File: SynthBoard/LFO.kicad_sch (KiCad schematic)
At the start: 33 parts, among them IC1 PIC16F15325-I/P, IC2 MCP6232T-E/SN, IC3 MCP6232T-E/SN, J3 Input, J4 Output, Q1 Q_NPN_ECB, U1 NJM4558M

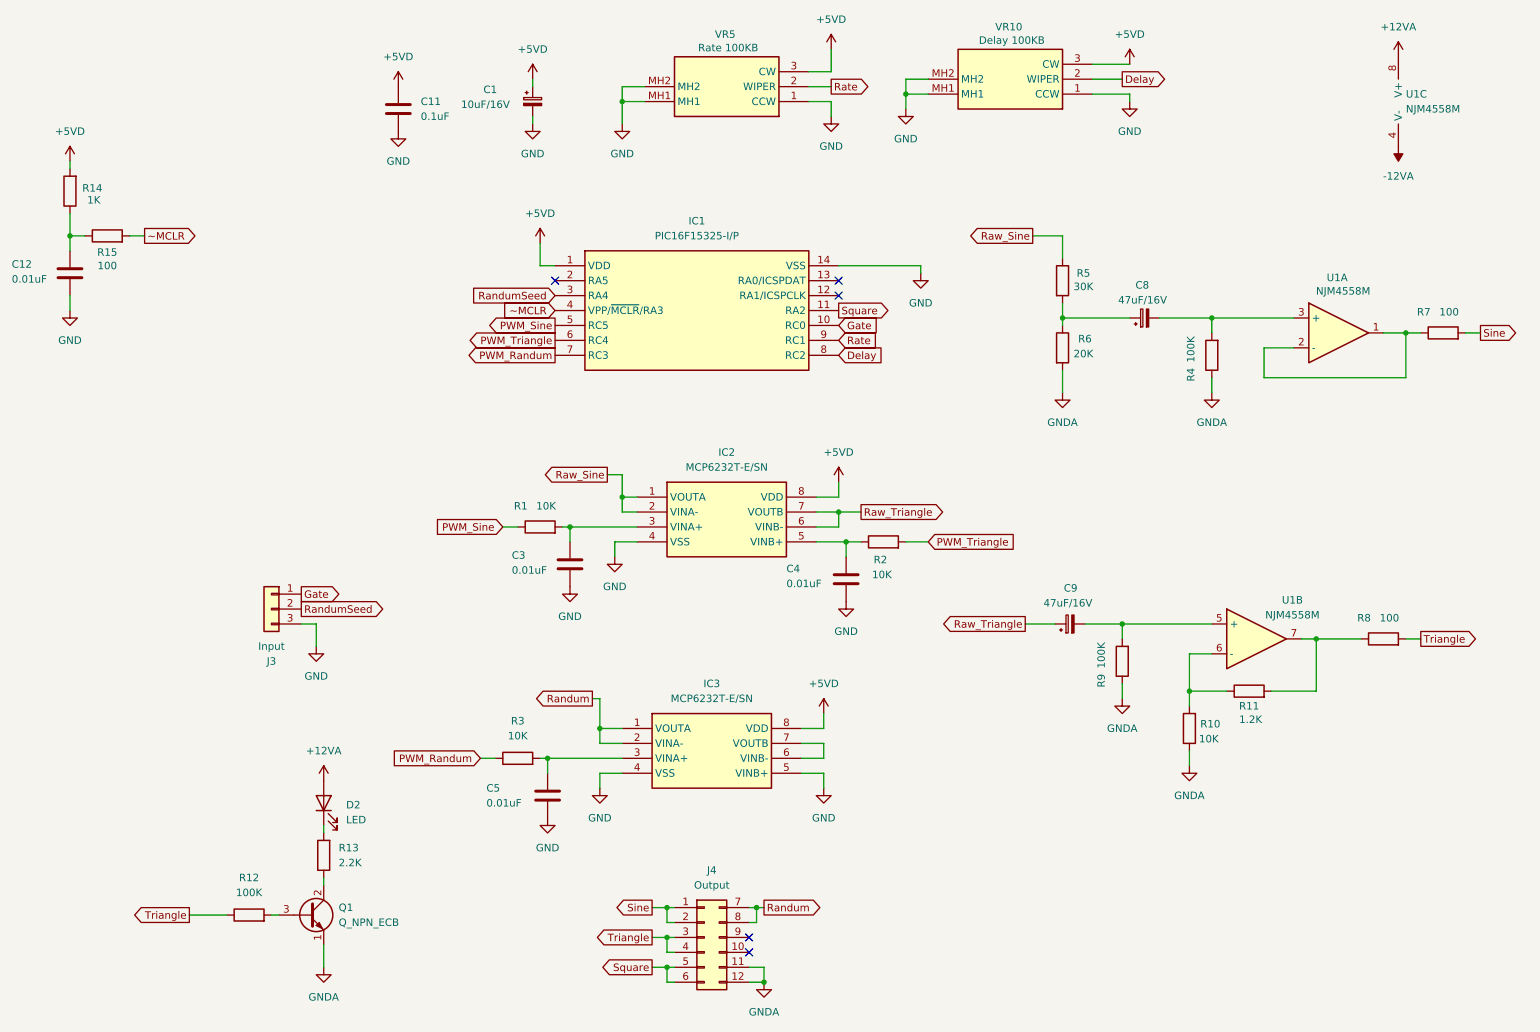
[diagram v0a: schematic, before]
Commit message: SynthBoard
部品をSMDにしてVCO+LFOを配置した
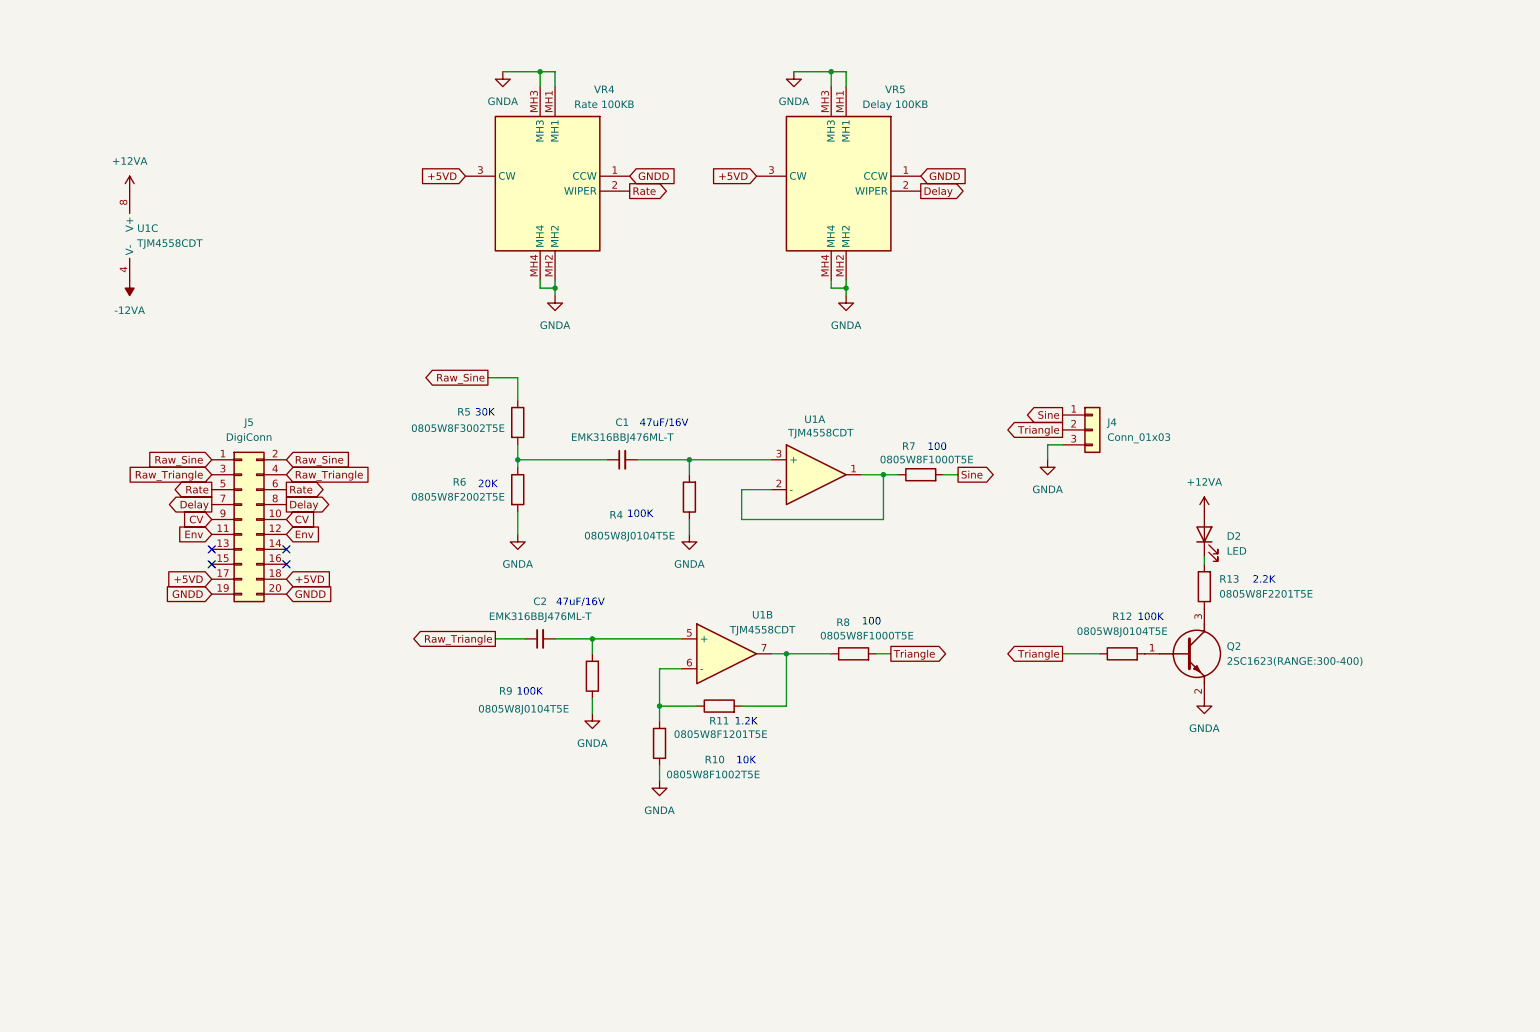
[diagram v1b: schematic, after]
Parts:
- removed C1: 10uF/16V, Capacitor_THT:CP_Radial_D5.0mm_P2.50mm, symbol Device:C_Polarized_Small
- removed C11: 0.1uF, Capacitor_SMD:C_0805_2012Metric_Pad1.18x1.45mm_HandSolder, symbol Device:C
- removed C12, C3, C4, C5: 0.01uF, Capacitor_THT:C_Disc_D7.5mm_W2.5mm_P5.00mm, symbol Device:C
- removed C8, C9: 47uF/16V, Capacitor_THT:CP_Radial_D5.0mm_P2.50mm, symbol Device:C_Polarized_Small
- removed IC1: PIC16F15325-I/P, Package_DIP:DIP-14_W7.62mm_LongPads, symbol SamacSys_Parts:PIC16F15325-I_P
- removed IC2, IC3: MCP6232T-E/SN, Package_SO:SOIC-8_3.9x4.9mm_P1.27mm, symbol SamacSys_Parts:MCP6232-E_P
- removed J3: Input, Connector_PinSocket_2.54mm:PinSocket_1x03_P2.54mm_Vertical, symbol Connector_Generic:Conn_01x03
- removed J4: Output, Connector_PinSocket_2.54mm:PinSocket_2x06_P2.54mm_Vertical, symbol Connector_Generic:Conn_02x06_Top_Bottom
- removed Q1: Q_NPN_ECB, Package_TO_SOT_THT:TO-92L_HandSolder, symbol Transistor_BJT:Q_NPN_ECB
- removed R1, R2, R3: 10K, Resistor_THT:R_Axial_DIN0204_L3.6mm_D1.6mm_P2.54mm_Vertical, symbol Device:R
- removed R14: 1K, Resistor_THT:R_Axial_DIN0204_L3.6mm_D1.6mm_P2.54mm_Vertical, symbol Device:R
- removed R15: 100, Resistor_THT:R_Axial_DIN0204_L3.6mm_D1.6mm_P2.54mm_Vertical, symbol Device:R
- removed VR10: Delay 100KB, SamacSys_parts:RK09D117000B, symbol SamacSys_Parts:RK09D117000B
- removed VR5: Rate 100KB, SamacSys_parts:RK09D117000B, symbol SamacSys_Parts:RK09D117000B
- added C1, C2: EMK316BBJ476ML-T, Capacitor_SMD:C_1206_3216Metric_Pad1.33x1.80mm_HandSolder, symbol Device:C_Small
- added J4: Conn_01x03, Connector_PinSocket_2.54mm:PinSocket_1x03_P2.54mm_Vertical, symbol Connector_Generic:Conn_01x03
- added J5: DigiConn, Connector_PinSocket_2.54mm:PinSocket_2x10_P2.54mm_Vertical, symbol Connector_Generic:Conn_02x10_Odd_Even
- added Q2: 2SC1623(RANGE:300-400), SamacSys_parts:SOT95P237X125-3N, symbol SamacSys_Parts:2SC1623-A
- added VR4: Rate 100KB, SamacSys_parts:PTA20432010CIB104, symbol SamacSys_Parts:PTA2043-2010CIB104
- added VR5: Delay 100KB, SamacSys_parts:PTA20432010CIB104, symbol SamacSys_Parts:PTA2043-2010CIB104
- R10: value 10K -> 0805W8F1002T5E; footprint Resistor_THT:R_Axial_DIN0204_L3.6mm_D1.6mm_P2.54mm_Vertical -> Resistor_SMD:R_0805_2012Metric_Pad1.20x1.40mm_HandSolder
- R11: value 1.2K -> 0805W8F1201T5E; footprint Resistor_THT:R_Axial_DIN0204_L3.6mm_D1.6mm_P2.54mm_Vertical -> Resistor_SMD:R_0805_2012Metric_Pad1.20x1.40mm_HandSolder
- R12, R4, R9: value 100K -> 0805W8J0104T5E; footprint Resistor_THT:R_Axial_DIN0204_L3.6mm_D1.6mm_P2.54mm_Vertical -> Resistor_SMD:R_0805_2012Metric_Pad1.20x1.40mm_HandSolder
- R13: value 2.2K -> 0805W8F2201T5E; footprint Resistor_THT:R_Axial_DIN0204_L3.6mm_D1.6mm_P2.54mm_Vertical -> Resistor_SMD:R_0805_2012Metric_Pad1.20x1.40mm_HandSolder
- R5: value 30K -> 0805W8F3002T5E; footprint Resistor_THT:R_Axial_DIN0204_L3.6mm_D1.6mm_P2.54mm_Vertical -> Resistor_SMD:R_0805_2012Metric_Pad1.20x1.40mm_HandSolder
- R6: value 20K -> 0805W8F2002T5E; footprint Resistor_THT:R_Axial_DIN0204_L3.6mm_D1.6mm_P2.54mm_Vertical -> Resistor_SMD:R_0805_2012Metric_Pad1.20x1.40mm_HandSolder
- R7, R8: value 100 -> 0805W8F1000T5E; footprint Resistor_THT:R_Axial_DIN0204_L3.6mm_D1.6mm_P2.54mm_Vertical -> Resistor_SMD:R_0805_2012Metric_Pad1.20x1.40mm_HandSolder
- U1: value NJM4558M -> TJM4558CDT
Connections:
- net +5VD: now also J5.17 (Pin_17), J5.18 (Pin_18), VR4.3 (CW), VR5.3 (CW)
- net Delay: now also J5.7 (Pin_7), J5.8 (Pin_8), VR5.2 (WIPER)
- net GNDA: now also J4.3 (Pin_3), Q2.2 (E), VR4.MH1, VR4.MH2, VR4.MH3, VR4.MH4, VR5.MH1, VR5.MH2, VR5.MH3, VR5.MH4
- net Rate: now also J5.5 (Pin_5), J5.6 (Pin_6), VR4.2 (WIPER)
- net Raw_Sine: now also J5.1 (Pin_1), J5.2 (Pin_2)
- net Raw_Triangle: now also C2.1, J5.3 (Pin_3), J5.4 (Pin_4)
- net Sine: now also J4.1 (Pin_1)
- net Triangle: now also J4.2 (Pin_2)
- net at R5.2, R6.1: now also C1.1
- net at R4.2, U1.3 (+): now also C1.2
- net at R9.2, U1.5 (+): now also C2.2
- net at R13.1: now also Q2.3 (C)
- net at R12.2: now also Q2.1 (B)
- new net CV: J5.10 (Pin_10), J5.9 (Pin_9)
- new net Env: J5.11 (Pin_11), J5.12 (Pin_12)
- new net GNDD: J5.19 (Pin_19), J5.20 (Pin_20), VR4.1 (CCW), VR5.1 (CCW)
- no-connect marks 5 -> 4
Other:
- note added: "1.2K"
- note added: "100"
- note added: "100K"
- note added: "10K"
- note added: "2.2K"
- note added: "20K"
- note added: "30K"
- note added: "47uF/16V"
- moved on the sheet: D2, R10, R11, R12, R13, R4, R5, R6, R7, R8, R9, U1A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

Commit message: SynthBorad
デジタルも配置した
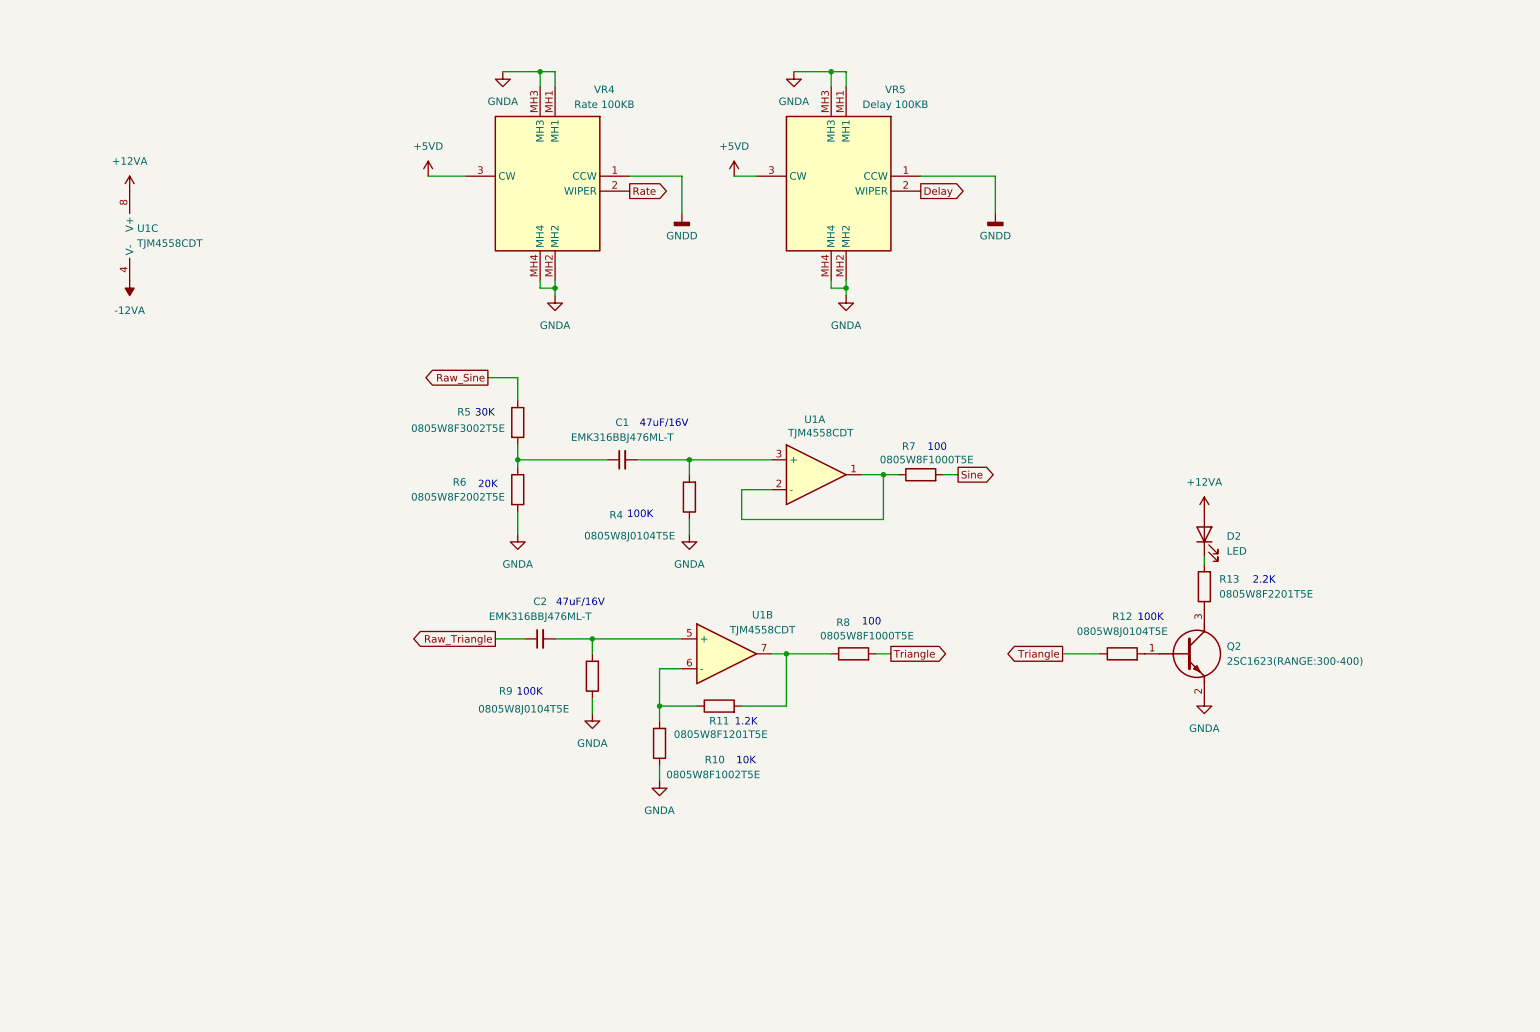
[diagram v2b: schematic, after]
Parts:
- removed J4: Conn_01x03, Connector_PinSocket_2.54mm:PinSocket_1x03_P2.54mm_Vertical, symbol Connector_Generic:Conn_01x03
- removed J5: DigiConn, Connector_PinSocket_2.54mm:PinSocket_2x10_P2.54mm_Vertical, symbol Connector_Generic:Conn_02x10_Odd_Even
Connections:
- no-connect marks 4 -> 0
